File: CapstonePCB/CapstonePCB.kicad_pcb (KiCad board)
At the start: 2 copper layers, 30 parts, among them J1 Conn_02x40_Counter_Clockwise, J2 Barrel_Jack, SW1 SW_Push, U1 NUCLEO64-F411RE, U2 LP-MSPM0G3507, U3 STSPIN220, U4 SN74AHC14N, U5 LM7805_TO220, U6 TLV1117-33, U8 APDS-9306

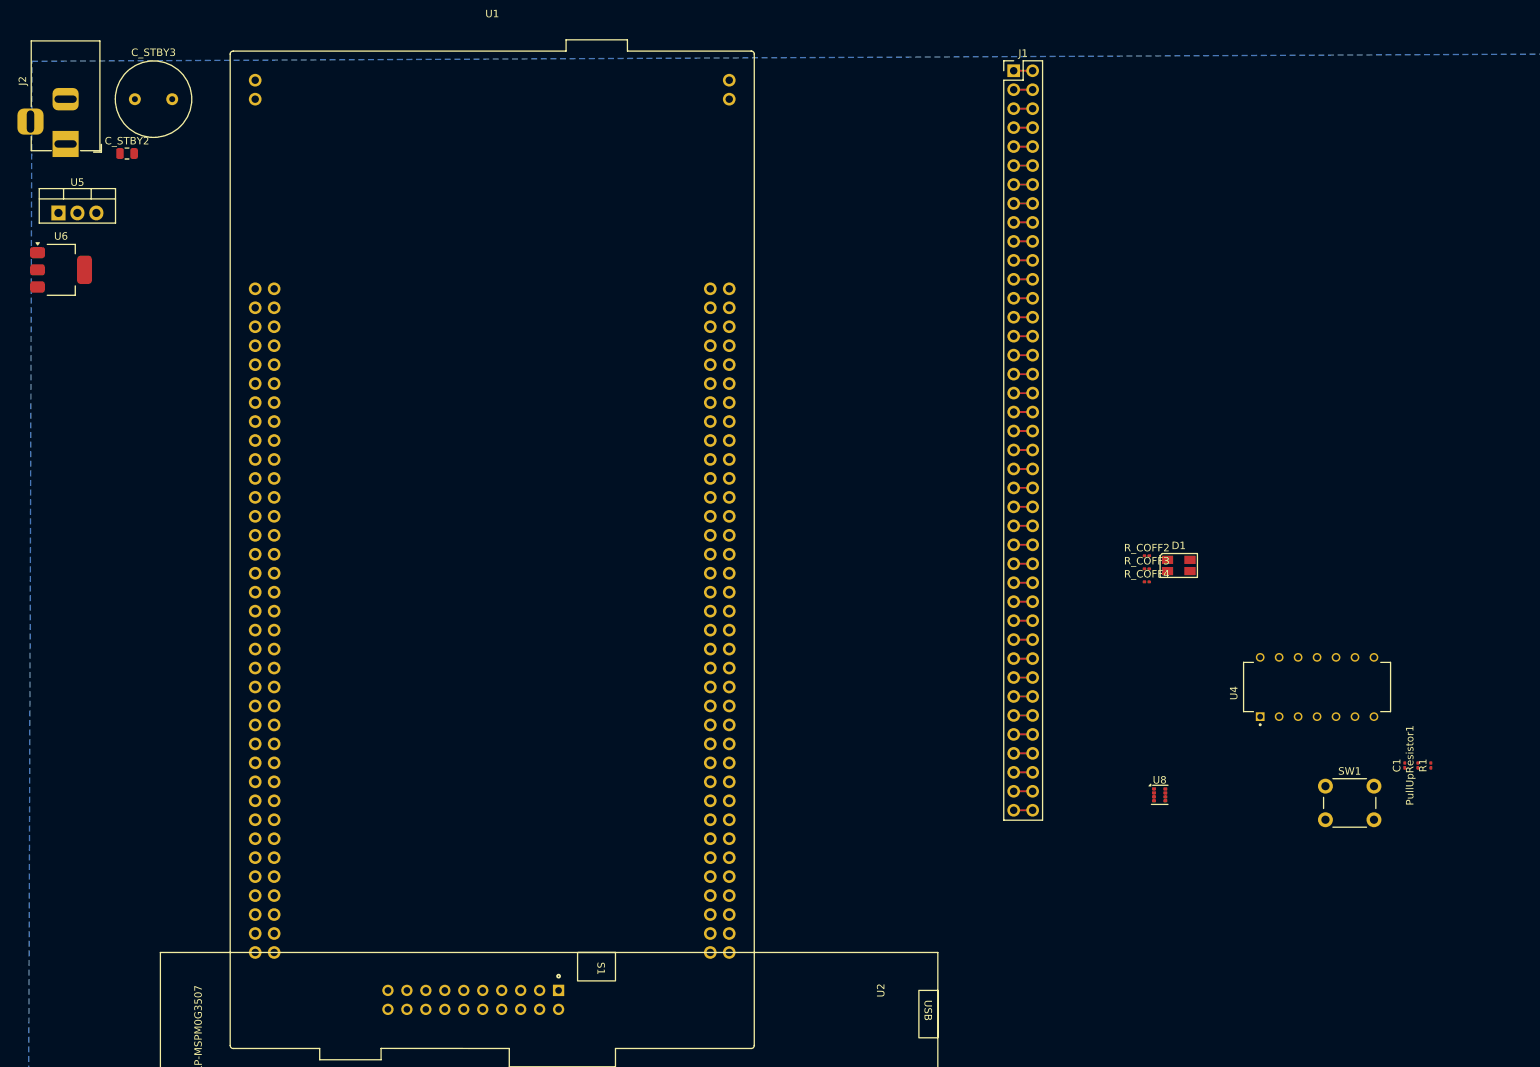
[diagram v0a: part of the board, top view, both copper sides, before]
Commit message: Updated routing for PCB
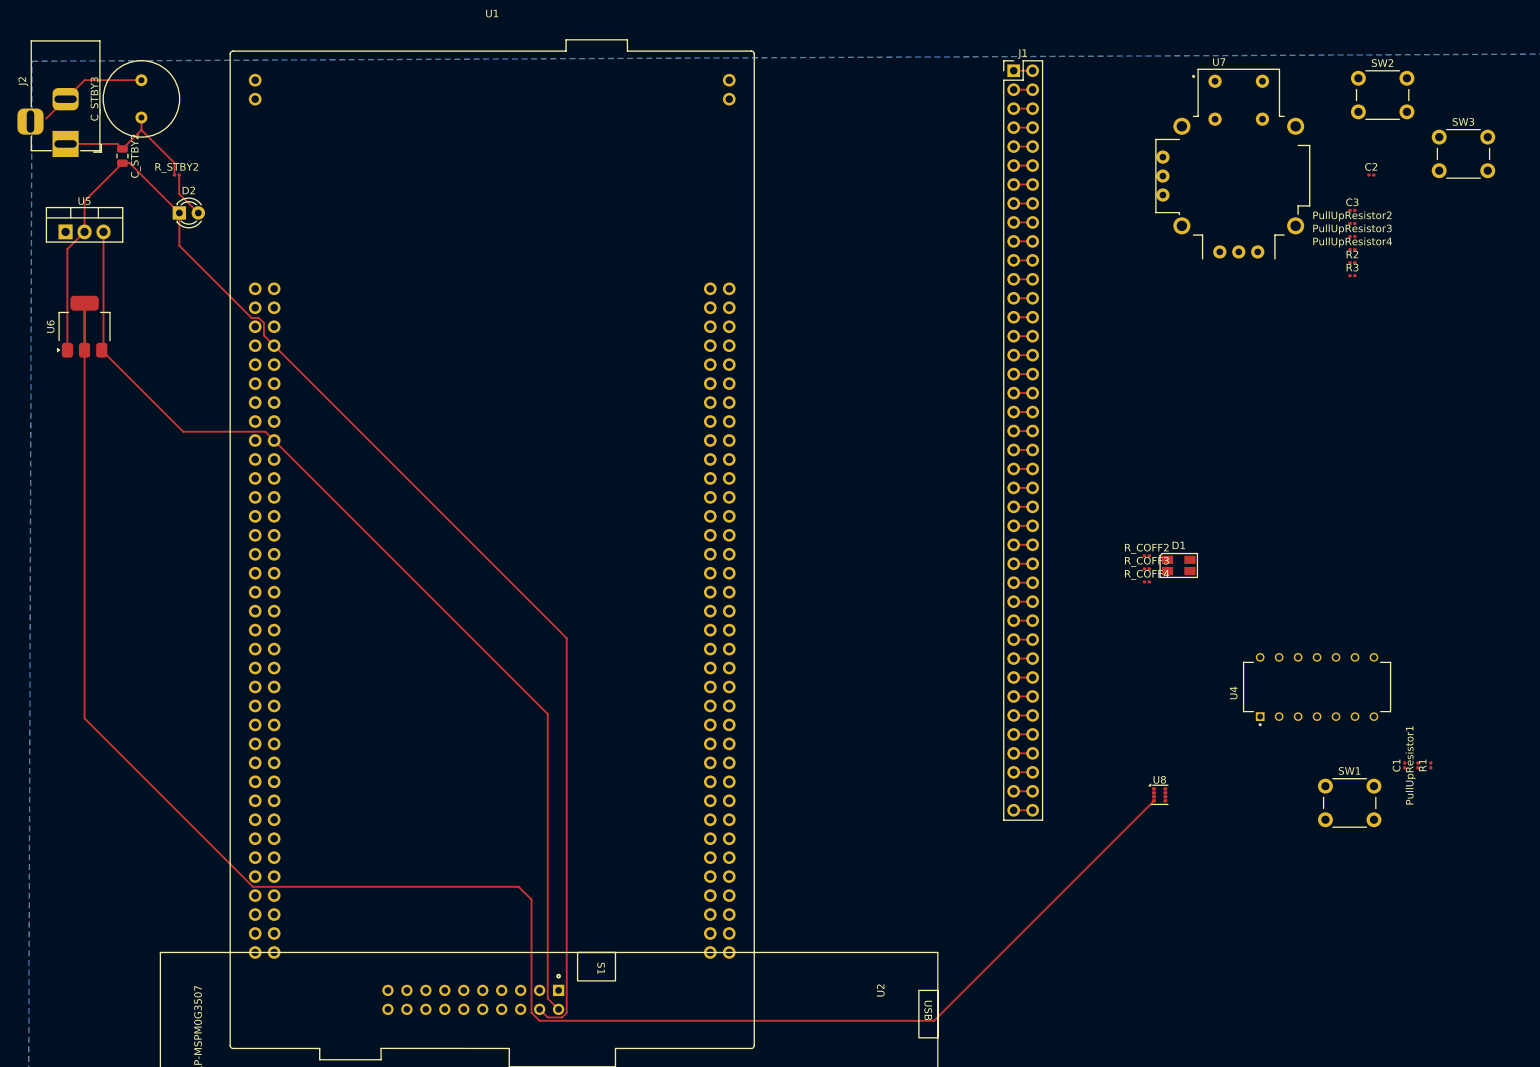
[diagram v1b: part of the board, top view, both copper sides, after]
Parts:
- added C2: 0.47 uF, Capacitor_SMD:C_0201_0603Metric, F.Cu at (195.2, 30.5)
- added C3: 0.47 uF, Capacitor_SMD:C_0201_0603Metric, F.Cu at (192.7, 35.2)
- added D2: LED, LED_THT:LED_D3.0mm_FlatTop, F.Cu at (35.6, 35.6)
- added PullUpResistor2: 10 kOhm, Resistor_SMD:R_0201_0603Metric, F.Cu at (192.7, 37.0)
- added PullUpResistor3: 10 kOhm, Resistor_SMD:R_0201_0603Metric, F.Cu at (192.7, 38.7)
- added PullUpResistor4: 10 kOhm, Resistor_SMD:R_0201_0603Metric, F.Cu at (192.7, 40.5)
- added R2: 10 kOhm, Resistor_SMD:R_0201_0603Metric, F.Cu at (192.7, 42.2)
- added R3: 10 kOhm, Resistor_SMD:R_0201_0603Metric, F.Cu at (192.7, 44.0)
- added R_STBY2: 5.5k ohm, Resistor_SMD:R_0201_0603Metric, F.Cu at (35.2, 30.5)
- added SW2: SW_Push, Button_Switch_THT:SW_PUSH_6mm_H7.3mm, F.Cu at (193.5, 17.5)
- added SW3: SW_Push, Button_Switch_THT:SW_PUSH_6mm_H7.3mm, F.Cu at (204.3, 25.4)
- added U7: COM-09032, Joystick:XDCR_COM-09032, F.Cu at (177.5, 30.6)
- moved U6 8.25 mm to (22.9, 50.8), turned to 90 degrees
- moved U5 2.71 mm to (20.3, 38.1)
- moved C_STBY3 2.61 mm to (30.5, 22.8), turned to 90 degrees
- moved C_STBY2 0.70 mm to (27.9, 27.9), turned to -90 degrees
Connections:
- net /Button Input renamed /Button1 Input
- net Net-(J1-Pin_67) renamed /Button No Debouning
- C1 pad 1: Net-(U4-1A) -> GNDREF
- C1 pad 2: GNDREF -> Net-(U4-1A)
- J1 pad 27: Net-(J1-Pin_27) -> GNDREF
- J1 pad 28: Net-(J1-Pin_27) -> GNDREF
- U3 pad 1: unconnected-(U3-DIR-Pad1) -> Net-(J1-Pin_35)
- U3 pad 11: unconnected-(U3-REF-Pad11) -> GNDREF
- U3 pad 15: unconnected-(U3-MODE2-Pad15) -> Net-(J1-Pin_29)
- U3 pad 16: unconnected-(U3-MODE1-Pad16) -> Net-(J1-Pin_31)
- U3 pad 2: unconnected-(U3-STCK-Pad2) -> Net-(J1-Pin_33)
- U3 pad 3: unconnected-(U3-OUTA1-Pad3) -> Net-(J1-Pin_37)
- U3 pad 5: unconnected-(U3-OUTA2-Pad5) -> Net-(J1-Pin_39)
- U4 pad 2: Net-(J1-Pin_41) -> Net-(J1-Pin_1)
- U4 pad 3: unconnected-(U4-2A-Pad3) -> Net-(U4-2A)
- U4 pad 4: unconnected-(U4-2Y-Pad4) -> Net-(J1-Pin_3)
- U4 pad 5: unconnected-(U4-3A-Pad5) -> Net-(U4-3A)
- U4 pad 6: unconnected-(U4-3Y-Pad6) -> Net-(J1-Pin_5)
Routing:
- net VDD: track 0.00 -> 243.0 mm
- net GNDREF: track 0.00 -> 189.5 mm
- net +5V: track 0.00 -> 136.0 mm
- net +12V: track 0.00 -> 21.0 mm
- net Net-(D2-A): track 0.00 -> 6.14 mm
- net Net-(J1-Pin_27): track 2.54 -> 0.00 mm

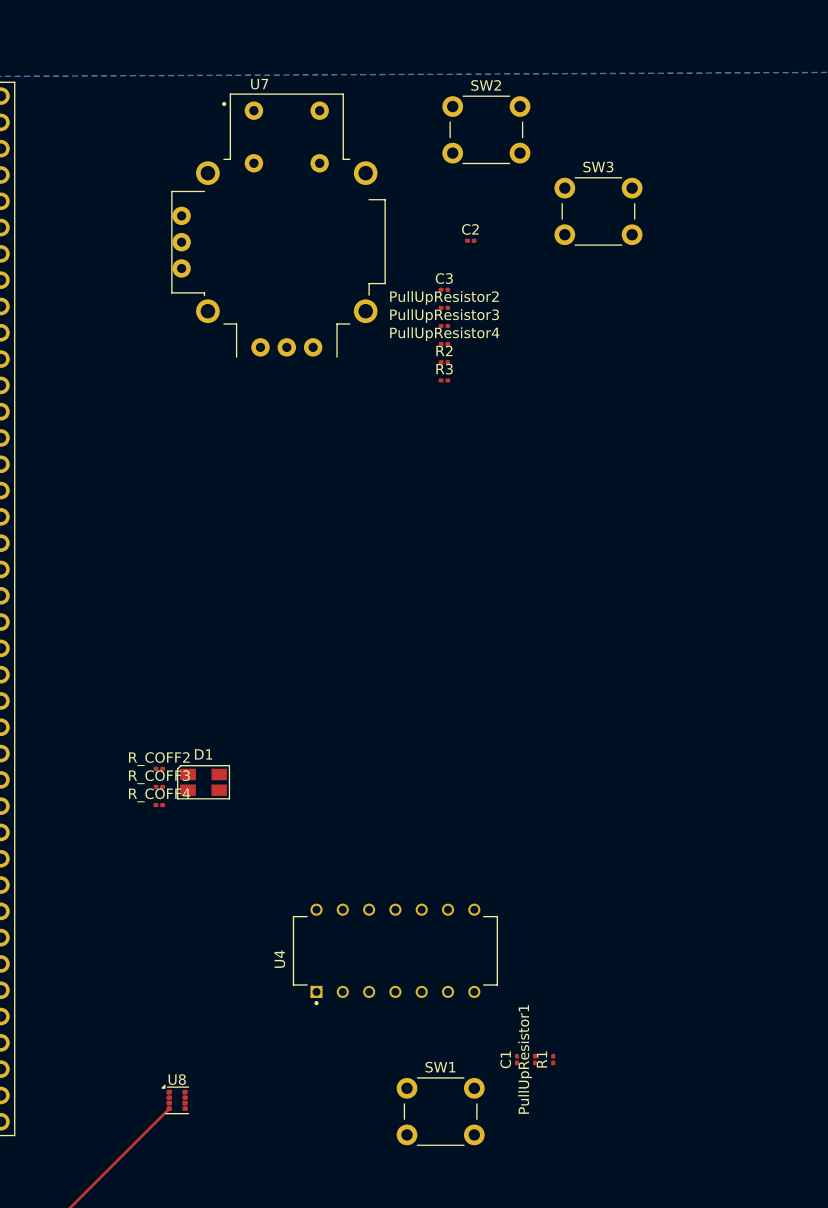
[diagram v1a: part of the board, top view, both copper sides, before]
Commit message: Additional routing for PCB
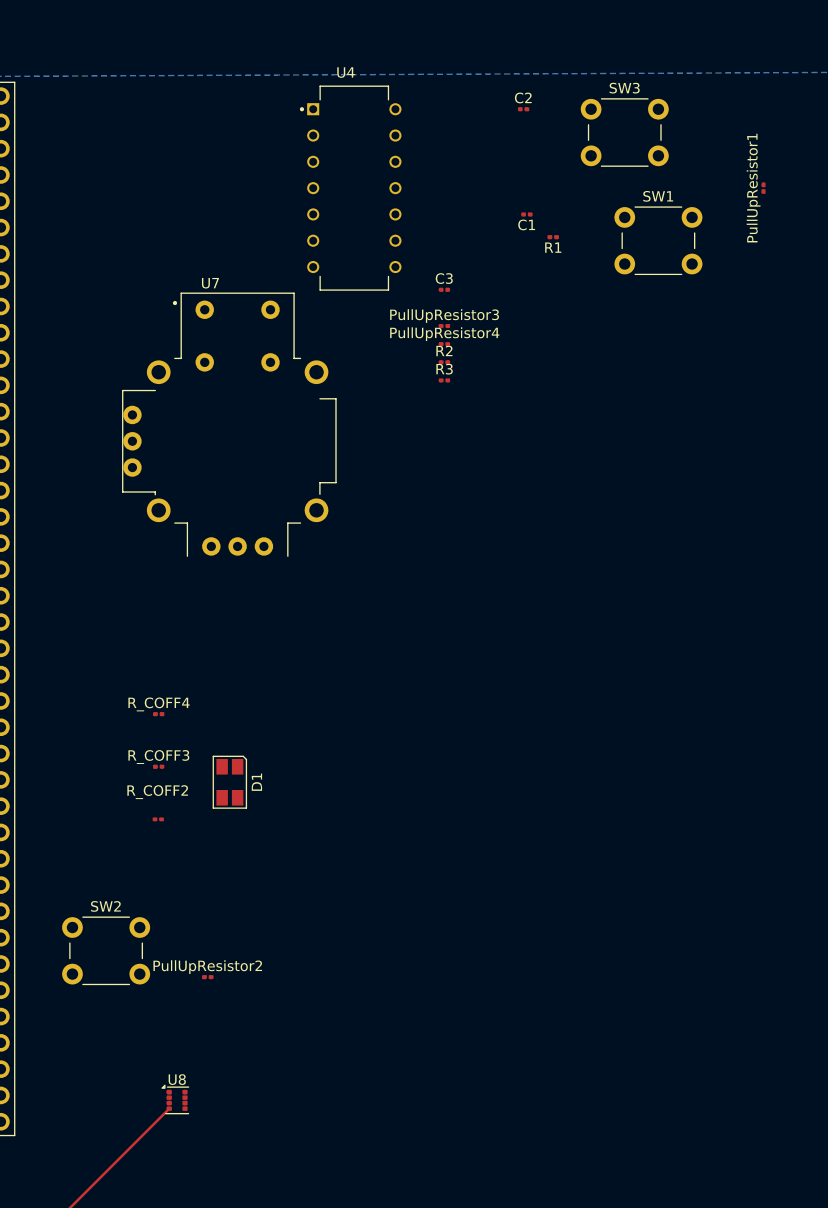
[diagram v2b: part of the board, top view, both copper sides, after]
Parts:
- moved SW2 87.4 mm to (156.8, 96.8)
- moved PullUpResistor1 87.0 mm to (223.5, 25.4)
- moved SW1 86.7 mm to (210.1, 28.2)
- moved C1 81.6 mm to (200.7, 27.9), turned to 180 degrees
- moved R1 79.4 mm to (203.2, 30.1), turned to 180 degrees
- moved U4 73.8 mm to (184.0, 25.4), turned to 0 degrees
- moved PullUpResistor2 68.6 mm to (169.8, 101.6)
- moved U7 19.8 mm to (172.7, 49.8)
- moved C2 13.7 mm to (200.3, 17.8)
- moved R_COFF4 8.78 mm to (165.1, 76.2)
- moved SW3 8.03 mm to (206.9, 17.8)
- moved R_COFF2 4.88 mm to (165.1, 86.4)
- moved D1 2.54 mm to (172.0, 82.8), turned to -90 degrees
- moved R_COFF3 1.95 mm to (165.1, 81.3)
